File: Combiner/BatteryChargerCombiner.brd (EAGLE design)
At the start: 220 x 42 mm, 148 parts, among them Q1 DMN6040SSD-13, Q2 DMN6040SSD-13, Q3 DMN6040SSD-13, Q4 DMN6040SSD-13, Q5 DMP4047SSD-13, Q6 220mA/50V/3.5Ω, Q7 220mA/50V/3.5Ω, U1 BQ24650, U10 TS7211, U11 MIC5219 3.3V, U12 MKR1000-SMD, U13 STWD100, U2 BQ28Z610, U3 BQ28Z610, U4 BQ24650, U5 TCA9543A, U6 WE-78, U7 WE-78, U8 74AHC1G07DBV, U9 74AUC1G06DBV

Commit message: All but four airwires routed
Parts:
- moved R35 266.8 mm to (179.7, 22.2), turned to 180 degrees
- moved R37 264.9 mm to (174.6, 29.2)
- moved R43 241.5 mm to (179.1, 36.8), turned to 180 degrees
- moved R44 235.3 mm to (166.4, 36.8)
- moved R40 232.5 mm to (174.6, 31.1), turned to 180 degrees
- moved R41 232.4 mm to (174.6, 33.0), turned to 180 degrees
- moved R24 231.4 mm to (118.7, 6.99), turned to 90 degrees
- moved R38 230.4 mm to (179.7, 24.1), turned to 180 degrees
- moved C15 227.8 mm to (104.1, 19.7)
- moved R39 225.7 mm to (171.4, 29.2)
- moved R23 225.2 mm to (116.8, 6.99), turned to 270 degrees
- moved C17 223.5 mm to (104.1, 2.54)
- moved C27 222.0 mm to (171.4, 31.1), turned to 180 degrees
- moved C14 221.2 mm to (95.9, 5.71), turned to 270 degrees
- moved R36 214.7 mm to (168.3, 24.8), turned to 90 degrees
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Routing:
- net VBAT2: track 113.4 -> 254.5 mm, vias 1 -> 3
- net AGND: track 0.00 -> 112.5 mm, vias 0 -> 8
- net VBAT1: track 165.3 -> 227.7 mm, vias 3 -> 6
- net N$19: track 0.00 -> 43.7 mm, vias 0 -> 6
- net N$36: track 0.00 -> 32.4 mm, vias 0 -> 2
- net N$20: track 0.00 -> 31.3 mm, vias 0 -> 3
- net SDA1: track 142.8 -> 113.6 mm
- net SCL1: track 143.5 -> 114.3 mm
- net N$27: track 0.00 -> 25.3 mm, vias 0 -> 2
- net N$43: track 0.00 -> 21.5 mm, vias 0 -> 2
- net N$13: track 0.00 -> 20.9 mm, vias 0 -> 2
- net N$21: track 0.00 -> 18.3 mm, vias 0 -> 2
- net BAT2: track 5.59 -> 23.3 mm, vias 0 -> 2
- net TS2: track 0.00 -> 16.1 mm, vias 0 -> 3
- net N$46: track 0.00 -> 16.0 mm, vias 0 -> 2
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- added copper zone on layer 16, net GND
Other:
- board size 220 x 42 mm -> 190.8 x 42 mm

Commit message: All signals routed. TODO: Add connectors for all temp sensors and board resistors for protection circuit sensors. Add power switching & fuses for all outputs.
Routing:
- net SCL2: track 13.7 -> 104.8 mm, vias 1 -> 6
- net SDA2: track 7.15 -> 95.7 mm, vias 1 -> 4
- net !BAT1_CE!: track 81.7 -> 157.8 mm, vias 2 -> 4
- net BAT1_STAT1: track 68.6 -> 141.4 mm, vias 1 -> 4
- net BAT1_STAT2: track 71.5 -> 139.6 mm, vias 1 -> 3
- net BAT2_STAT1: track 104.1 -> 146.9 mm, vias 2 -> 6
- net BAT2_STAT2: track 116.6 -> 157.7 mm, vias 2 -> 4
- net !BAT2_CE!: track 89.9 -> 116.2 mm
- net AGND: track 112.5 -> 111.8 mm

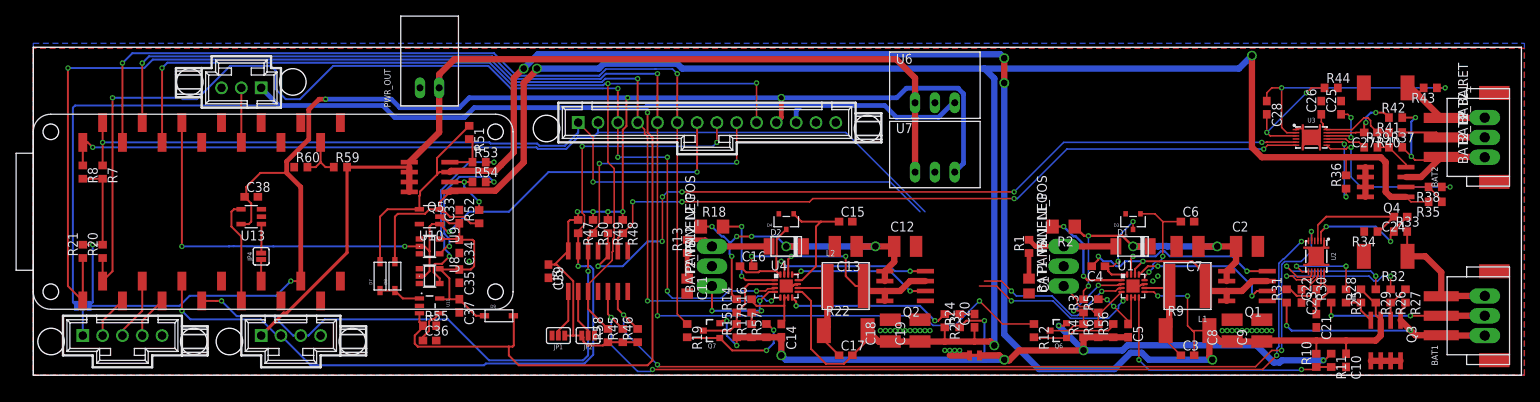
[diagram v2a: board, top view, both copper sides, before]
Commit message: Added temp sensor inputs, power switches, and mounting holes
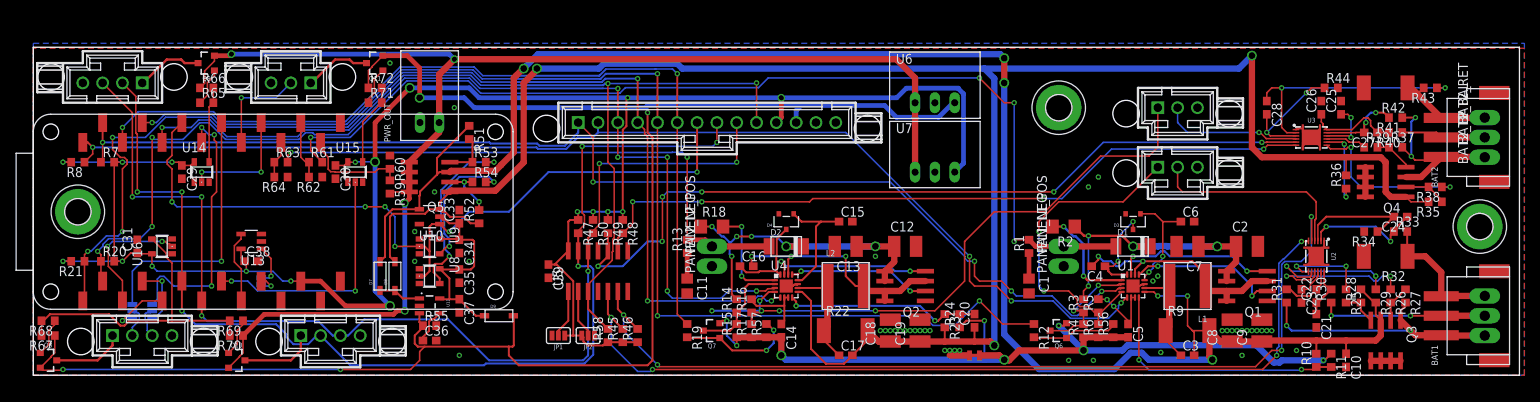
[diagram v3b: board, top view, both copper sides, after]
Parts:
- removed JP3: JUMPER-SMT_3_NO_SILK, SparkFun-Jumpers:SMT-JUMPER_3_NO_SILK
- added C29, C30, C31: (no value), resistor:C0603
- added H1, H2, H3: MOUNT-PAD-ROUND3.2, holes:3,2-PAD
- added JP5, JP6: JUMPER-SMT_3_NO_SILK, SparkFun-Jumpers:SMT-JUMPER_3_NO_SILK
- added MASTHEAD: HEADER_POS4_70545, con-molex-c-grid-sl:70545-POS4
- added Q10, Q11, Q8, Q9: 4.3A/20V/54mΩ, SparkFun-DiscreteSemi:SOT23-3
- added R61, R62, R63, R64: (no value), resistor:R0603
- added R65, R68, R69, R71: 100R, resistor:R0603
- added R66, R67, R70, R72: 10M, resistor:R0603
- added U14, U15, U16: 74AUC1G06DBV, 74xx-little-us:SOT23-5
- BAT1_TS, BAT2_TS: value TPPAD1-13Y -> HEADER_POS3_70545; device testpad:P1-13Y -> con-molex-c-grid-sl:70545-POS3
- ROTATION: value HEADER_POS5_70545 -> HEADER_POS4_70545; device con-molex-c-grid-sl:70545-POS5 -> con-molex-c-grid-sl:70545-POS4
- moved BAT2_TS 63.9 mm to (146.7, 34.3), turned to 180 degrees
- moved BAT1_TS 21.1 mm to (146.7, 26.7), turned to 180 degrees
- moved R60 11.4 mm to (45.7, 27.3), turned to 270 degrees
- moved C38 8.25 mm to (27.9, 14.6)
- moved R59 6.84 mm to (45.7, 24.1), turned to 270 degrees
- moved TAIL 6.38 mm to (33.0, 37.5)
- moved ANEMOMETER 5.08 mm to (38.1, 5.08)
- moved PWR_OUT 4.45 mm to (50.8, 32.4)
- moved JP4 3.18 mm to (29.2, 12.1), flipped to the bottom
- moved U13 3.18 mm to (27.9, 17.1)
- moved ROTATION 2.54 mm to (14.0, 5.08)
- moved R20 1.42 mm to (9.53, 14.6), turned to 0 degrees
- moved R21 1.42 mm to (5.71, 14.6), turned to 180 degrees
- moved R7 1.42 mm to (9.53, 27.3), turned to 0 degrees
- moved R8 1.42 mm to (5.71, 27.3), turned to 180 degrees
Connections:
- removed net BAT1_TS: U2.4
- removed net BAT2_TS: U3.4
- removed net MOSI: ROTATION.P$2, U12.D8
- removed net TS1: BAT1_TS.TP, R5.1, R6.2, U1.4
- removed net TS2: BAT2_TS.TP, R16.1, R17.2, U4.4
- new net BAT1_TS1: BAT1_TS.P$1, R5.1, R6.2, U1.4
- new net BAT1_TS2: BAT1_TS.P$2, U2.4
- new net BAT2_TS1: BAT2_TS.P$1, R16.1, R17.2, U4.4
- new net BAT2_TS2: BAT2_TS.P$2, U3.4
- new net COS: JP6.1, U12.A6
- new net MASTHEAD_PWR: U12.A3, U14.2
- new net N$47: JP6.2, ROTATION.P$3
- new net N$49: JP5.2, ROTATION.P$2
- new net N$53: Q8.1, R68.1
- new net N$56: R63.1, R64.2, U12.A2
- new net N$58: MASTHEAD.P$1, Q9.3
- new net N$63: Q9.1, R65.1
- new net N$66: ANEMOMETER.P$1, Q10.3
- new net N$67: Q10.1, R69.1
- new net N$69: R67.2, R68.2, R69.2, R70.2, U16.4
- new net N$70: Q11.3, TAIL.P$1
- new net N$71: Q11.1, R71.1
- new net N$72: R71.2, R72.2, U15.4
- new net PANEL1: D1.A, PANEL1_POS.TP, R1.2, R61.2
- new net PANEL2: D2.A, PANEL2_POS.TP, R13.2, R63.2
- new net SENSOR_PWR: U12.D8, U16.2
- new net SERVO_PWR: U12.D13, U15.2
- new net SIN: JP5.1, U12.A5
- net +3V3: now also C29.1, C30.1, C31.1, U14.5, U15.5, U16.5; no longer JP3.1
- net +5V: now also Q11.2, Q8.2, R67.1, R72.1; no longer JP3.3, TAIL.P$1
- net GND: now also BAT1_TS.P$3, BAT2_TS.P$3, C29.2, C30.2, C31.2, H1.B3,2, H2.B3,2, H3.B3,2, MASTHEAD.P$4, R62.1, R64.1, ROTATION.P$4, U14.3, U15.3, U16.3; no longer ROTATION.P$5
- net MISO: now also JP5.3; no longer ROTATION.P$4
- net N$14: now also R61.1, R62.2, U12.A1; no longer D2.A, PANEL2_POS.TP, R13.2
- net N$2: now also Q8.3, ROTATION.P$1; no longer D1.A, PANEL1_POS.TP, R1.2
- net N$64: now also R65.2, R66.2, U14.4; no longer JP3.2, ROTATION.P$1
- net SCK: now also JP6.3; no longer ROTATION.P$3
- net SCL: now also MASTHEAD.P$3
- net SDA: now also MASTHEAD.P$2
- net VSELECT: now also Q10.2, Q9.2, R66.1, R70.1; no longer ANEMOMETER.P$1
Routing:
- net PANEL1: track 0.00 -> 131.0 mm, vias 0 -> 4
- net BAT2_TS1: track 0.00 -> 80.5 mm, vias 0 -> 5
- net PANEL2: track 0.00 -> 74.0 mm, vias 0 -> 2
- net VSELECT: track 125.9 -> 172.5 mm, vias 0 -> 4
- net BAT1_TS1: track 0.00 -> 41.3 mm, vias 0 -> 2
- net N$69: track 0.00 -> 40.7 mm
- net SCL: track 102.6 -> 142.1 mm, vias 4 -> 6
- net COS: track 0.00 -> 34.8 mm, vias 0 -> 3
- net SIN: track 0.00 -> 34.0 mm, vias 0 -> 1
- net SDA: track 108.9 -> 141.9 mm, vias 4 -> 6
- net SERVO_PWR: track 0.00 -> 31.6 mm, vias 0 -> 2
- net BAT1_TS2: track 0.00 -> 26.2 mm
- net +3V3: track 240.4 -> 259.5 mm, vias 9 -> 18
- net BAT2_TS2: track 0.00 -> 17.9 mm, vias 0 -> 1
- net SENSOR_PWR: track 0.00 -> 16.6 mm, vias 0 -> 2
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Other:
- board size 190.8 x 42 mm -> 190.5 x 42 mm

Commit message: Silkscreen cleaned up; ready for test
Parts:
- removed JP5, JP6: JUMPER-SMT_3_NO_SILK, SparkFun-Jumpers:SMT-JUMPER_3_NO_SILK
- added C32: 100n, resistor:C0603
- added R73, R74, R75, R76, R77, R78: (no value), resistor:R0603
- added U17: LMV358, SparkFun-IC-Amplifiers:SO08
- C29, C30, C31: value (none) -> 100n
- SYSTEM: value HEADER_POS14_70545 -> HEADER_POS15_70545; device con-molex-c-grid-sl:70545-POS14 -> con-molex-c-grid-sl:70545-POS15
- moved U6 9.86 mm to (118.1, 25.4)
- moved U7 9.25 mm to (118.1, 34.9)
- moved BAT2_TS 1.91 mm to (146.7, 36.2)
- moved SYSTEM 1.27 mm to (87.6, 32.4)
- moved ANEMOMETER 0.63 mm to (38.1, 4.45)
- moved ROTATION 0.63 mm to (14.0, 4.45)
- renumbered JP4 to WDT-RST
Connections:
- removed net N$14: R61.1, R62.2, U12.A1
- removed net N$47: JP6.2, ROTATION.P$3
- removed net N$49: JP5.2, ROTATION.P$2
- removed net N$56: R63.1, R64.2, U12.A2
- new net COS_IN: R75.2, ROTATION.P$3
- new net N$62: R73.1, R74.2, U17.2
- new net N$73: R75.1, R76.2, U17.6
- new net N$78: R77.1, R78.2, U17.3, U17.5
- new net PANEL1_DIV: R61.1, R62.2, SYSTEM.P$13, U12.A1
- new net PANEL2_DIV: R63.1, R64.2, SYSTEM.P$14, U12.A2
- new net SIN_IN: R73.2, ROTATION.P$2
- net +3V3: now also C32.1, R77.2, U17.8
- net COS: now also R76.1, U17.7; no longer JP6.1
- net GND: now also C32.2, R78.1, SYSTEM.P$15, U17.4; no longer SYSTEM.P$13, SYSTEM.P$14
- net MISO: no longer JP5.3
- net SCK: no longer JP6.3
- net SIN: now also R74.1, U17.1; no longer JP5.1
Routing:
- net PANEL2_DIV: track 0.00 -> 92.4 mm, vias 0 -> 6
- net PANEL1_DIV: track 0.00 -> 82.4 mm, vias 0 -> 4
- net SIN_IN: track 0.00 -> 29.4 mm, vias 0 -> 3
- net COS_IN: track 0.00 -> 25.5 mm, vias 0 -> 1
- net N$73: track 0.00 -> 24.6 mm, vias 0 -> 2
- net SIN: track 34.0 -> 19.8 mm, vias 1 -> 4
- net N$62: track 0.00 -> 12.4 mm, vias 0 -> 2
- net +3V3: track 259.5 -> 269.3 mm
- net N$78: track 0.00 -> 9.59 mm, vias 0 -> 2
- net SCK: track 7.98 -> 0.00 mm, vias 1 -> 0
- net N$14: track 7.66 -> 0.00 mm
- net MISO: track 7.59 -> 0.00 mm, vias 1 -> 0
- net +5V: track 218.1 -> 223.5 mm
- net N$56: track 4.79 -> 0.00 mm
- net COS: track 34.8 -> 30.2 mm, vias 3 -> 6
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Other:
- board text added: "+"
- board text added: "-"
- board text added: "ANEMOMETER"
- board text added: "BAT1 TEMP"
- board text added: "BAT2 TEMP"
- board text added: "MASTHEAD"
- board text added: "PANEL1+"
- board text added: "PANEL1-"
- board text added: "PANEL2+"
- board text added: "PANEL2-"
- board text added: "ROTATION"
- board text added: "SERVO"
- board text added: "SYSTEM"

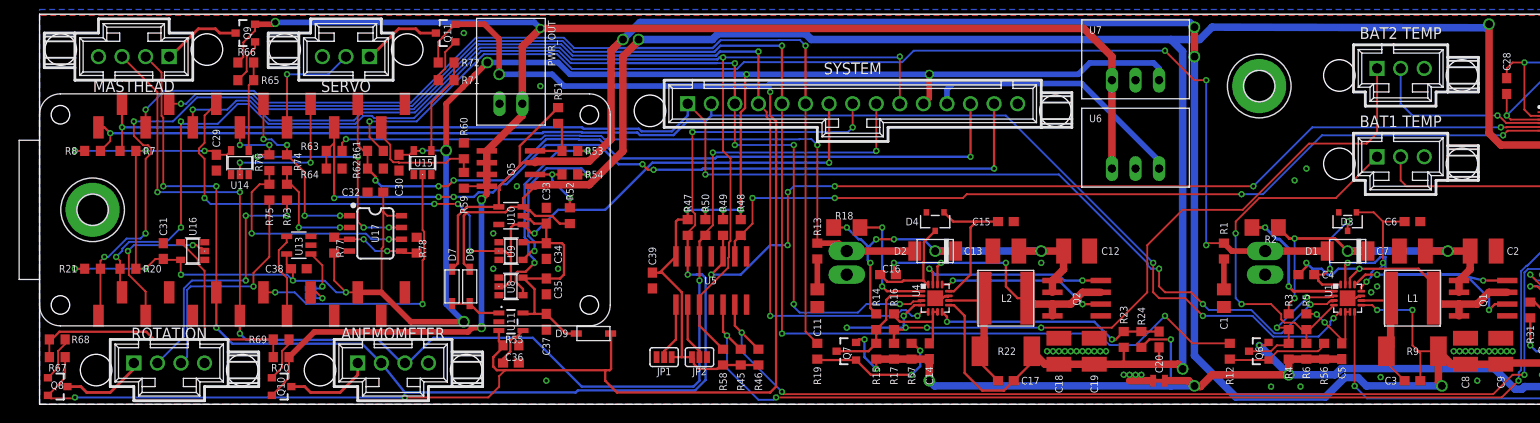
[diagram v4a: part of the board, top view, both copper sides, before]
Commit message: Now with selectable control schemes for the masthead light -- either I2C or PWM dimming & Neopixel
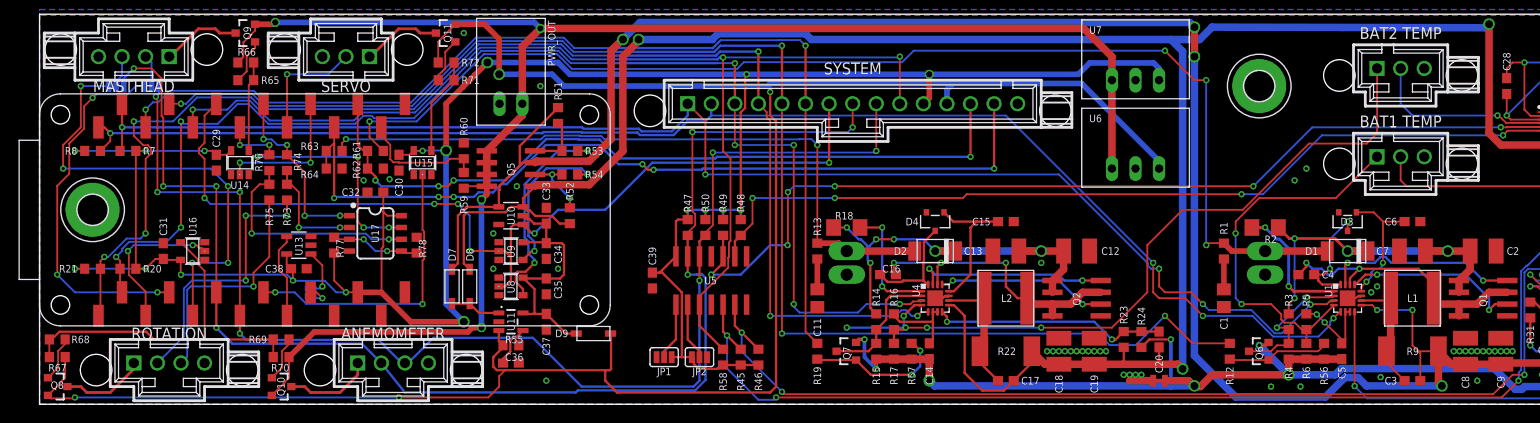
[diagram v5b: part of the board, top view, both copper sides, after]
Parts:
- added JP3, JP4: JUMPER-SMT_3_NO_SILK, SparkFun-Jumpers:SMT-JUMPER_3_NO_SILK
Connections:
- removed net MISO: U12.D10
- removed net SCK: U12.D9
- new net DIM: JP4.3, U12.D10
- new net N$14: JP3.2, MASTHEAD.P$2
- new net N$47: JP4.2, MASTHEAD.P$3
- new net NEOPIXEL: JP3.3, U12.D9
- net SCL: now also JP3.1; no longer MASTHEAD.P$3
- net SDA: now also JP4.1; no longer MASTHEAD.P$2
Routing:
- net DIM: track 0.00 -> 49.1 mm, vias 0 -> 5
- net NEOPIXEL: track 0.00 -> 39.5 mm, vias 0 -> 3
- net SCL: track 142.7 -> 138.1 mm, vias 6 -> 7
- net N$47: track 0.00 -> 3.44 mm
- net N$14: track 0.00 -> 3.44 mm
- net SDA: track 141.0 -> 143.8 mm, vias 6 -> 7
- net N$5: track 21.9 -> 21.0 mm
- net GND: vias 43 -> 45

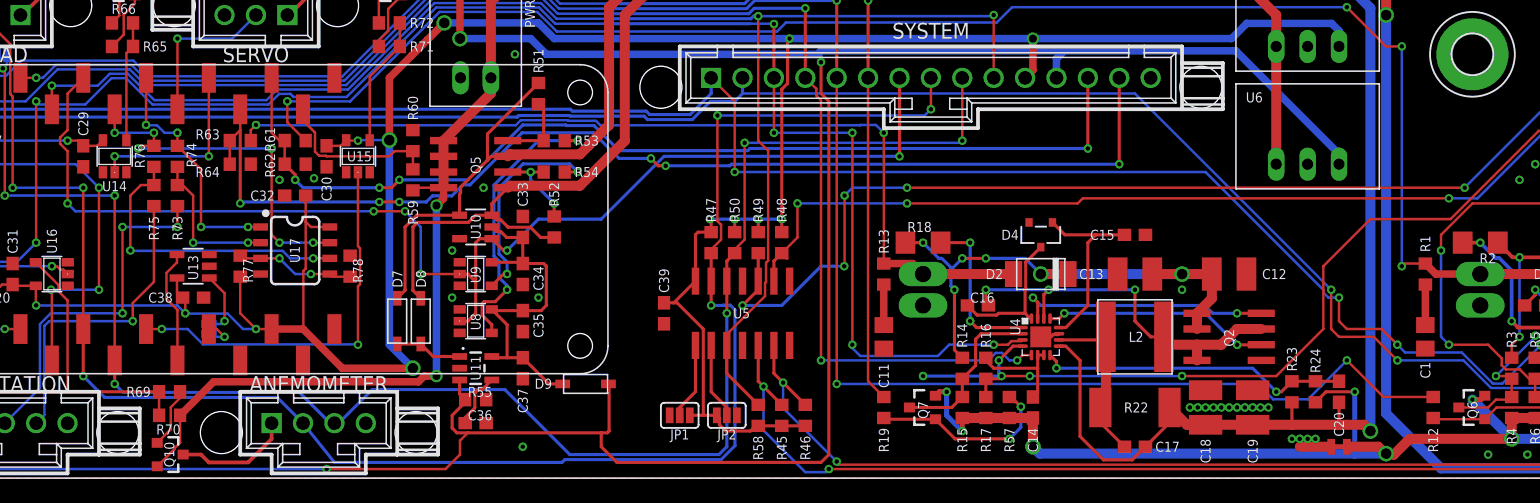
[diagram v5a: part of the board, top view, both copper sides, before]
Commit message: Rationalized some traces
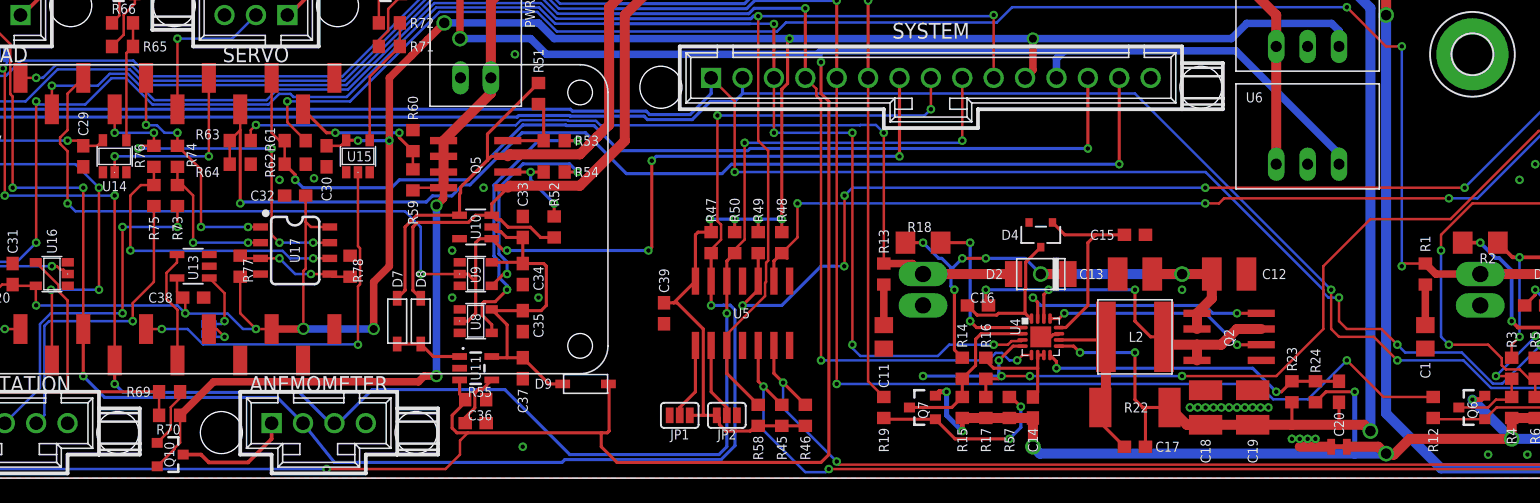
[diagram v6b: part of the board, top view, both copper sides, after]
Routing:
- net +3V3: track 269.3 -> 261.4 mm, vias 18 -> 19
- net BAT_SELECT: track 100.7 -> 104.8 mm
- net N$60: track 13.6 -> 12.0 mm, vias 0 -> 2
- net VBAT2: track 255.4 -> 254.3 mm, vias 3 -> 5
- net PANEL2_DIV: track 92.4 -> 92.9 mm, vias 6 -> 2
- net PANEL1_DIV: vias 4 -> 2
